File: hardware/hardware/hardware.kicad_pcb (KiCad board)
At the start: 2 copper layers, 16 parts, among them U1 PC817, U2 PC817, U3 PC817, U4 PC817

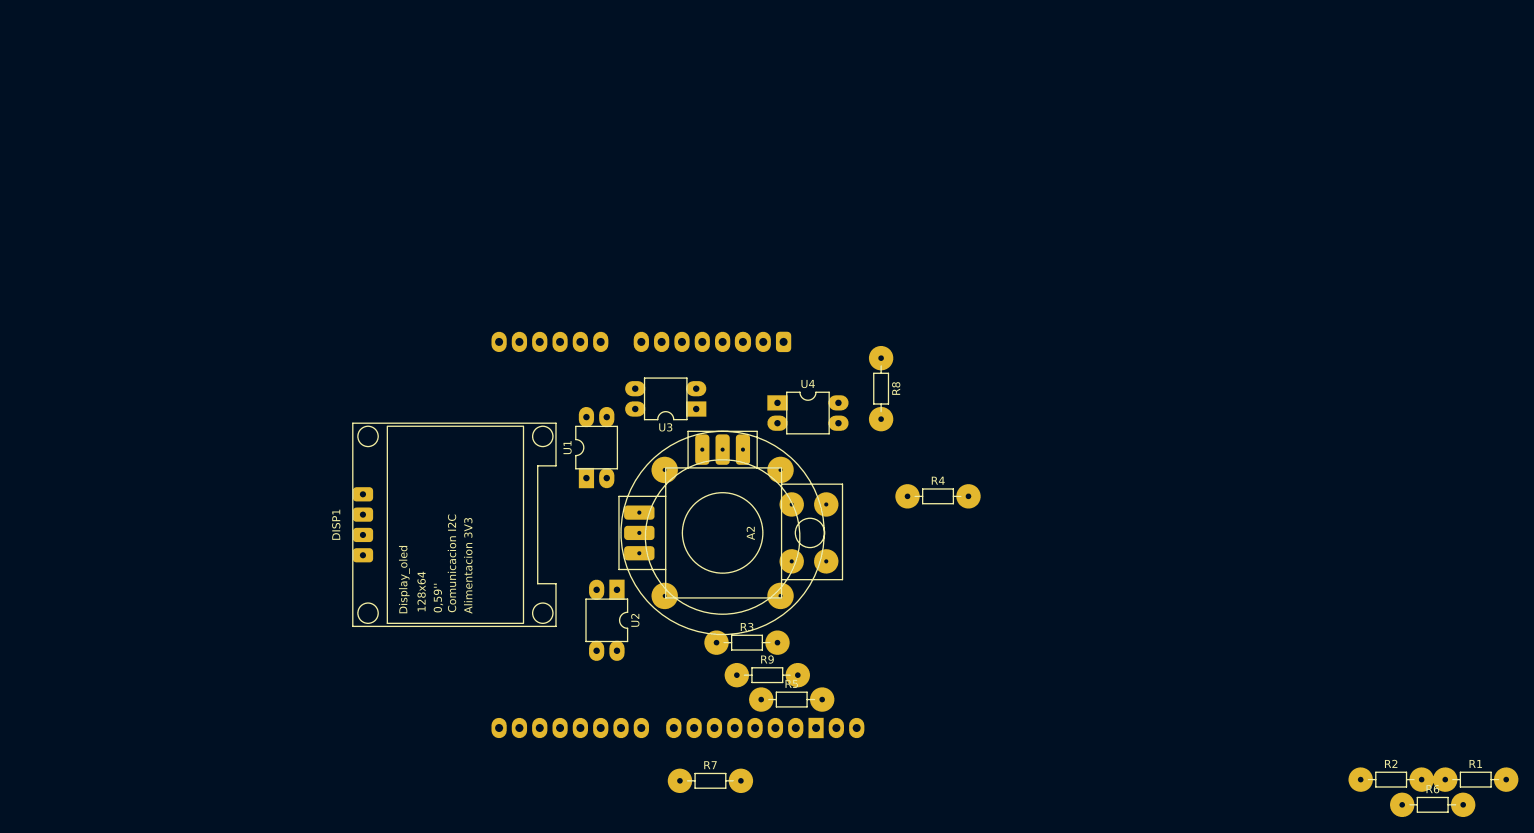
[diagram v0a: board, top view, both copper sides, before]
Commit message: solucionado problema que se paraba la viborita
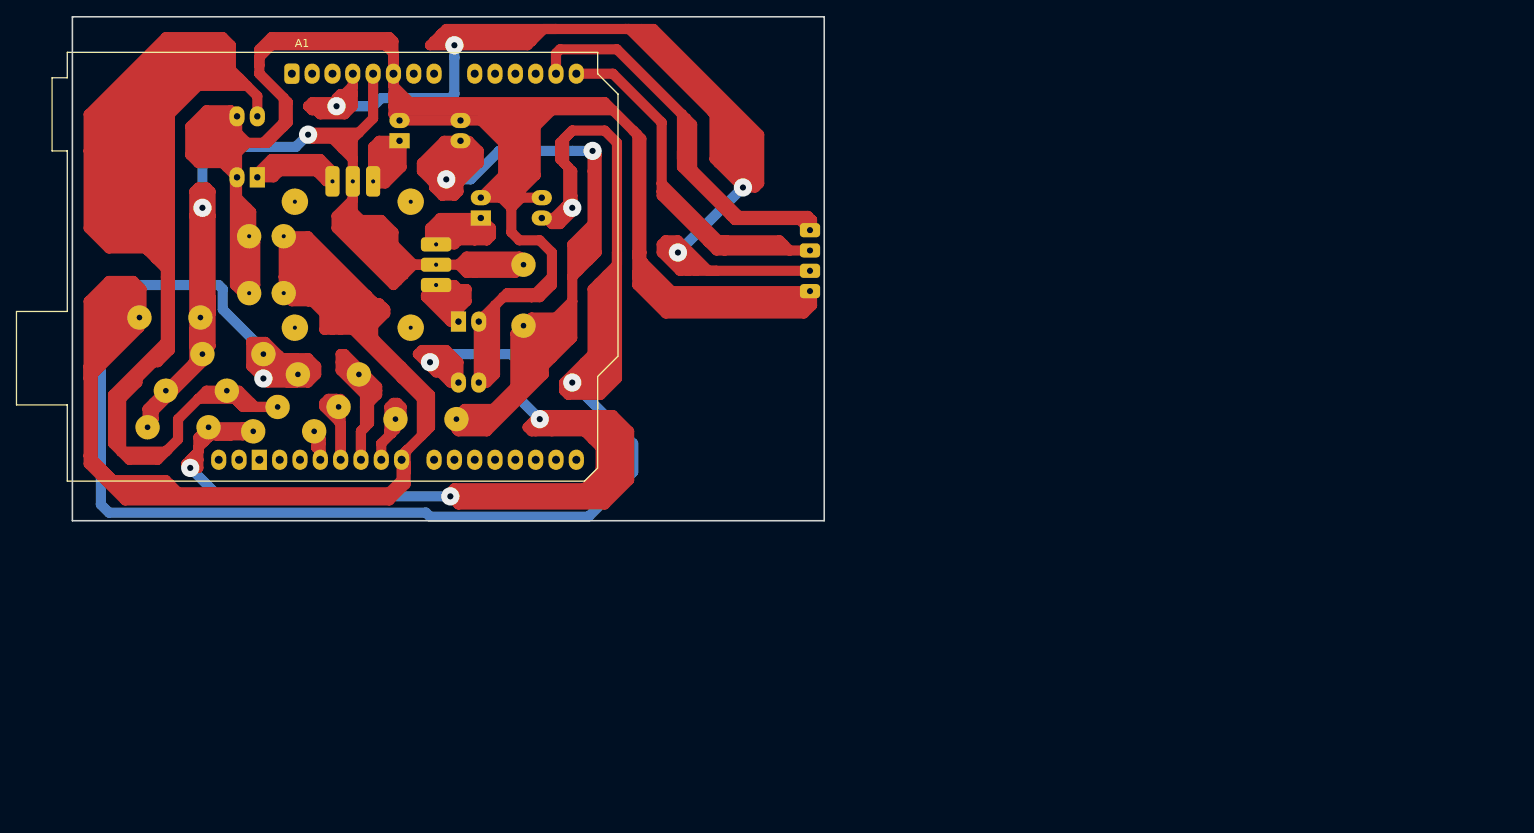
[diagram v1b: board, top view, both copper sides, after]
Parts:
- A1: moved to F.Cu
- A2, DISP1, R1, R2, R3, R4, R5, R6, R7, R8, R9, U1, U2, U3, U4: moved to B.Cu
- moved R1 166.0 mm to (17.0, 38.6), turned to 180 degrees
- moved R2 154.2 mm to (17.3, 43.2)
- moved R6 128.9 mm to (57.4, 32.0), turned to -90 degrees
- moved R4 95.4 mm to (10.4, 52.3)
- moved R8 89.5 mm to (12.7, 47.8), turned to 0 degrees
- moved U4 70.9 mm to (24.1, 21.1), turned to 90 degrees
- moved A1 70.0 mm to (28.4, 8.13), turned to 0 degrees
- moved R5 65.2 mm to (31.2, 52.8), turned to 180 degrees
- moved R9 60.0 mm to (34.3, 49.8), turned to 180 degrees
- moved R7 57.5 mm to (41.4, 51.3)
- moved A2 57.1 mm to (36.1, 32.0)
- moved R3 55.9 mm to (36.8, 45.7), turned to 180 degrees
- moved U3 50.0 mm to (41.9, 16.5), turned to 0 degrees
- moved DISP1 46.7 mm to (81.8, 31.5)
- moved U2 38.9 mm to (49.3, 39.1)
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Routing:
- net Net-(A1-Pad6): track 0.00 -> 544.5 mm
- net Net-(R8-Pad2): track 0.00 -> 488.4 mm
- net Net-(A1-Pad23): track 0.00 -> 402.7 mm
- net Net-(R2-Pad2): track 0.00 -> 333.7 mm, vias 0 -> 3
- net Net-(A1-Pad5): track 0.00 -> 292.9 mm, vias 0 -> 2
- net Net-(A1-Pad4): track 0.00 -> 280.1 mm, vias 0 -> 4
- net Net-(R4-Pad2): track 0.00 -> 267.8 mm, vias 0 -> 4
- net Net-(R6-Pad2): track 0.00 -> 238.6 mm, vias 0 -> 1
- net Net-(A1-Pad13): track 0.00 -> 85.8 mm
- net Net-(A1-Pad14): track 0.00 -> 82.2 mm
- net Net-(A1-Pad25): track 0.00 -> 43.3 mm
- net Net-(A2-Pad4): track 0.00 -> 40.2 mm
- net Net-(A2-Pad6): track 0.00 -> 35.8 mm
- net Net-(A2-Pad1): track 0.00 -> 34.1 mm
- net Net-(A2-Pad3): track 0.00 -> 33.5 mm
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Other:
- board outline added: 94 x 63 mm
